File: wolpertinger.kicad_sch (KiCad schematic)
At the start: 57 parts, among them IC1 TL074, IC2 TL074, K1 FRT5, K2 FRT5, Q1 BC549, T1 IN LEFT, T2 IN RIGHT, T3 SWT, T4 SWT, T5 OUT LEFT, T6 OUT RIGHT, T7 LED+, T8 LED-, U1 4093, U2 VTL5C, U3 VTL5C, U4 VTL5C, U5 VTL5C

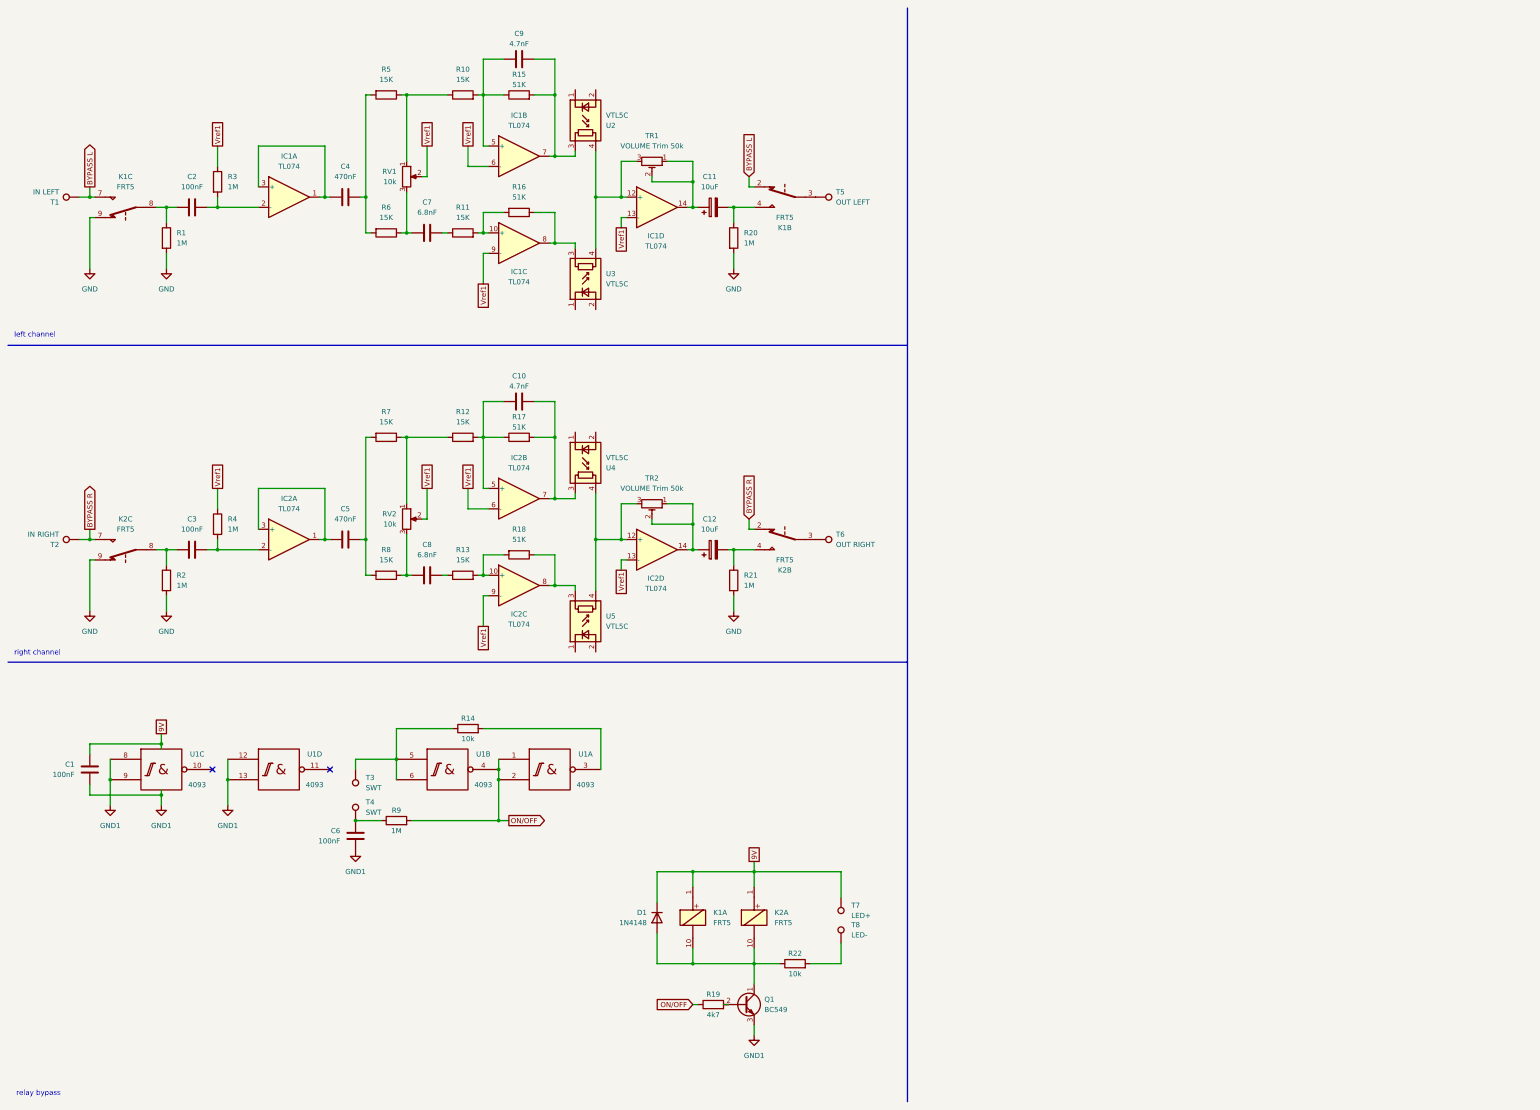
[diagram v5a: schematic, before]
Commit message: add power supply
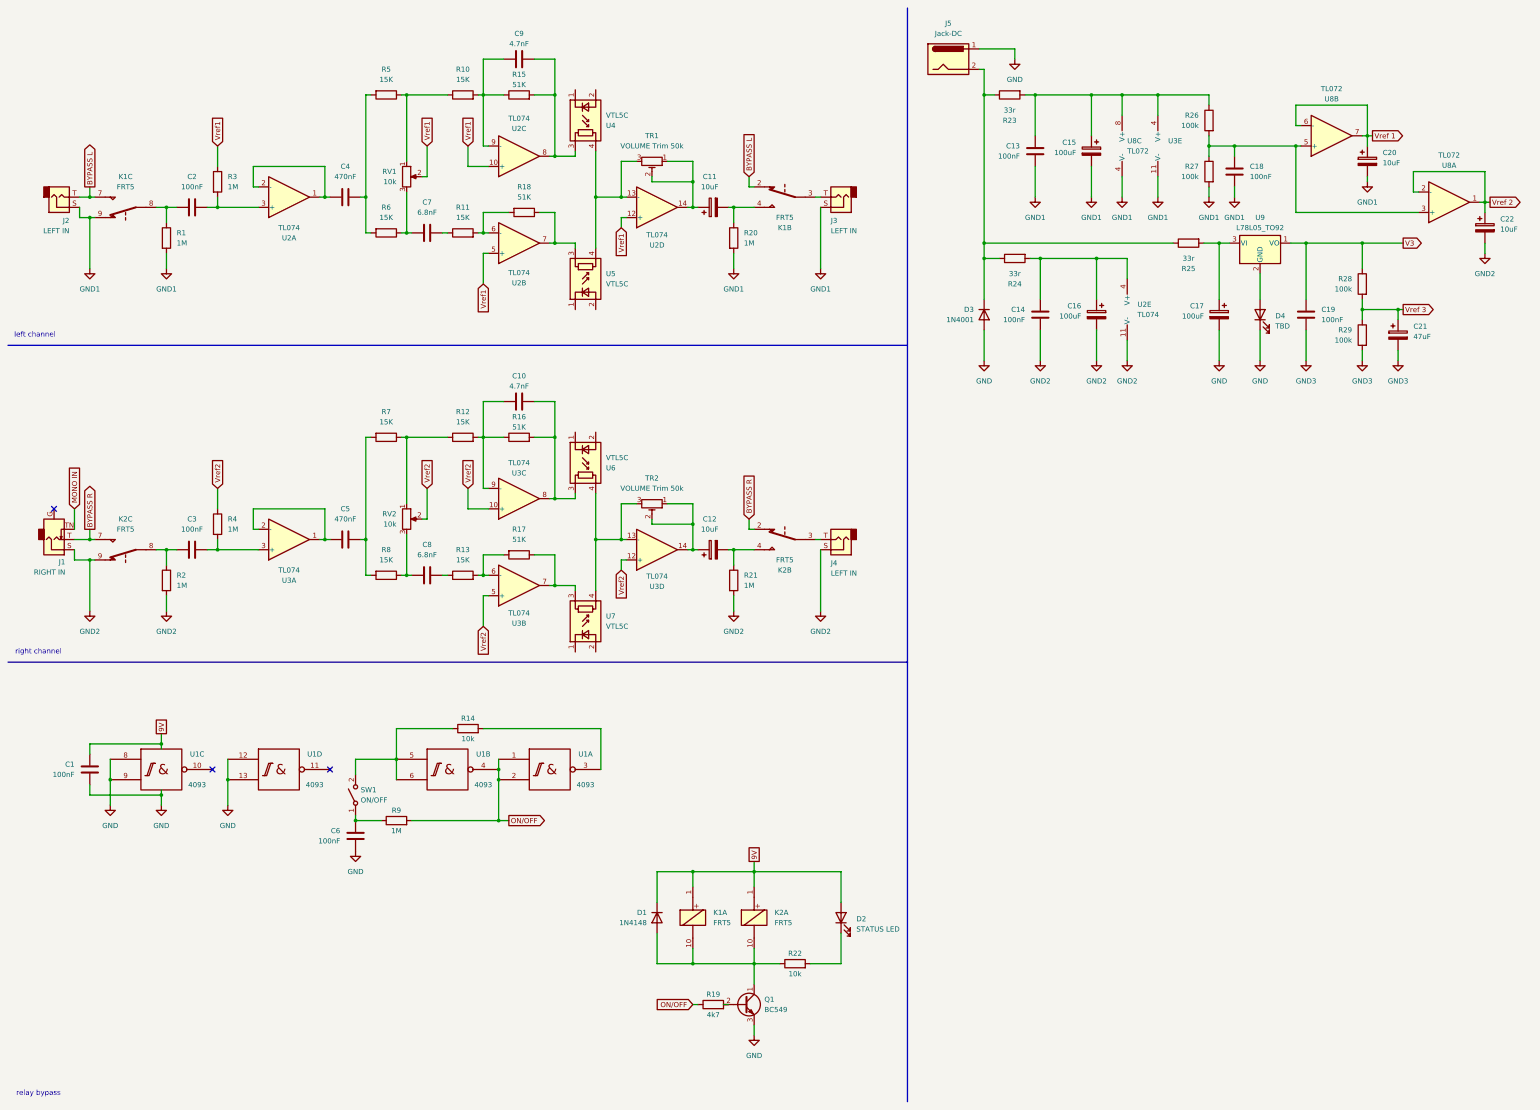
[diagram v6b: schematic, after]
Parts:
- removed IC1, IC2: TL074, Package_DIP:CERDIP-14_W7.62mm_SideBrazed_LongPads_Socket, symbol Amplifier_Operational:TL074
- removed T1: IN LEFT, Connector_Wire:SolderWire-0.5sqmm_1x01_D0.9mm_OD2.1mm, symbol Connector:TestPoint
- removed T2: IN RIGHT, Connector_Wire:SolderWire-0.5sqmm_1x01_D0.9mm_OD2.1mm, symbol Connector:TestPoint
- removed T3, T4: SWT, Connector_Wire:SolderWire-0.5sqmm_1x01_D0.9mm_OD2.1mm, symbol Connector:TestPoint
- removed T5: OUT LEFT, Connector_Wire:SolderWire-0.5sqmm_1x01_D0.9mm_OD2.1mm, symbol Connector:TestPoint
- removed T6: OUT RIGHT, Connector_Wire:SolderWire-0.5sqmm_1x01_D0.9mm_OD2.1mm, symbol Connector:TestPoint
- removed T7: LED+, Connector_Wire:SolderWire-0.5sqmm_1x01_D0.9mm_OD2.1mm, symbol Connector:TestPoint
- removed T8: LED-, Connector_Wire:SolderWire-0.5sqmm_1x01_D0.9mm_OD2.1mm, symbol Connector:TestPoint
- added C13, C14, C18, C19: 100nF, symbol Device:C
- added C15, C16, C17: 100uF, symbol Device:C_Polarized
- added C20, C22: 10uF, symbol Device:C_Polarized
- added C21: 47uF, symbol Device:C_Polarized
- added D2: STATUS LED, symbol Device:LED
- added D3: 1N4001, Diode_THT:D_DO-41_SOD81_P10.16mm_Horizontal, symbol Diode:1N4001
- added D4: TBD, symbol Device:LED
- added J1: RIGHT IN, symbol Connector_Audio:NRJ4HH-1
- added J2, J3, J4: LEFT IN, symbol Connector_Audio:NJ2FD-V
- added J5: Jack-DC, symbol Connector:Jack-DC
- added R23, R24, R25: 33r, Resistor_THT:R_Axial_DIN0207_L6.3mm_D2.5mm_P7.62mm_Horizontal, symbol Device:R
- added R26, R27, R28, R29: 100k, Resistor_THT:R_Axial_DIN0207_L6.3mm_D2.5mm_P7.62mm_Horizontal, symbol Device:R
- added SW1: ON/OFF, symbol Switch:SW_SPST
- added U2, U3: TL074, symbol Amplifier_Operational:TL074
- added U8: TL072, symbol Amplifier_Operational:TL072
- added U9: L78L05_TO92, Package_TO_SOT_THT:TO-92_Inline, symbol Regulator_Linear:L78L05_TO92
- renumbered R17 to R16, R18 to R17, R16 to R18, U2 to U4, U3 to U5, U4 to U6, U5 to U7
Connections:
- net BYPASS L: now also J2.T
- net BYPASS R: now also J1.T
- net GND: now also C1.2, C6.2, Q1.3 (E), U1.12, U1.13, U1.7 (Vss), U1.7 (Vss), U1.7 (Vss), U1.7 (Vss), U1.8, U1.9, C17.2, D3.2 (A), D4.1 (K), J5.1; no longer K1.9, K2.9, R1.2, R2.2, R20.2, R21.2
- net GND1: now also K1.9, R1.2, R20.2, C13.1, C15.2, C18.1, C20.2, J2.S, J3.S, R27.2, U3.11 (V-), U8.4 (V-); no longer C1.2, C6.2, Q1.3 (E), U1.12, U1.13, U1.7 (Vss), U1.7 (Vss), U1.7 (Vss), U1.7 (Vss), U1.8, U1.9
- net Vdd: now also D2.2 (A)
- net Vref1: now also U2.10 (+), U2.12 (+), U2.5 (+); no longer R4.1, RV2.2
- net at C9.1, R10.2, R15.1: now also U2.9 (-)
- net at K2.3: now also J4.T
- net at TR2.3, U6.4, U7.4: now also U3.13 (-)
- net at C12.1, TR2.1, TR2.2: now also U3.14
- net at C9.2, R15.2, U4.3: now also U2.8
- net at TR1.3, U4.4, U5.4: now also U2.13 (-)
- net at C4.1: now also U2.1, U2.2 (-)
- net at C2.2, R3.2: now also U2.3 (+)
- net at R14.1, U1.5, U1.6: now also SW1.2 (B)
- net at R17.1, U7.3: now also U3.7
- net at C10.2, R16.2, U6.3: now also U3.8
- net at C5.1: now also U3.1, U3.2 (-)
- net at C3.2, R4.2: now also U3.3 (+)
- net at R22.2: now also D2.1 (K)
- net at C6.1, R9.1: now also SW1.1 (A)
- net at K1.3: now also J3.T
- net at R13.2, R17.2: now also U3.6 (-)
- net at C11.1, TR1.1, TR1.2: now also U2.14
- net at R11.2, R18.2: now also U2.6 (-)
- net at R18.1, U5.3: now also U2.7
- net at C10.1, R12.2, R16.1: now also U3.9 (-)
- new net: C18.2, R26.2, R27.1, U8.3 (+), U8.5 (+)
- new net: D4.2 (A), U9.2 (GND)
- new net: C17.1, R25.2, U9.3 (VI)
- new net: C13.2, C15.1, R23.2, R26.1, U3.4 (V+), U8.8 (V+)
- new net: D3.1 (K), J5.2, R23.1, R24.1, R25.1
- new net: C14.2, C16.1, R24.2, U2.4 (V+)
- new net GND2: C14.1, C16.2, C22.2, J1.S, J4.S, K2.9, R2.2, R21.2, U2.11 (V-)
- new net GND3: C19.1, C21.2, R29.2
- new net MONO IN: J1.TN
- new net V3: C19.2, R28.1, U9.1 (VO)
- new net Vref 1: C20.1, U8.6 (-), U8.7
- new net Vref 2: C22.1, U8.1, U8.2 (-)
- new net Vref 3: C21.1, R28.2, R29.1
- new net Vref2: R4.1, RV2.2, U3.10 (+), U3.12 (+), U3.5 (+)
- no-connect marks 2 -> 3
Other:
- moved on the sheet: R18

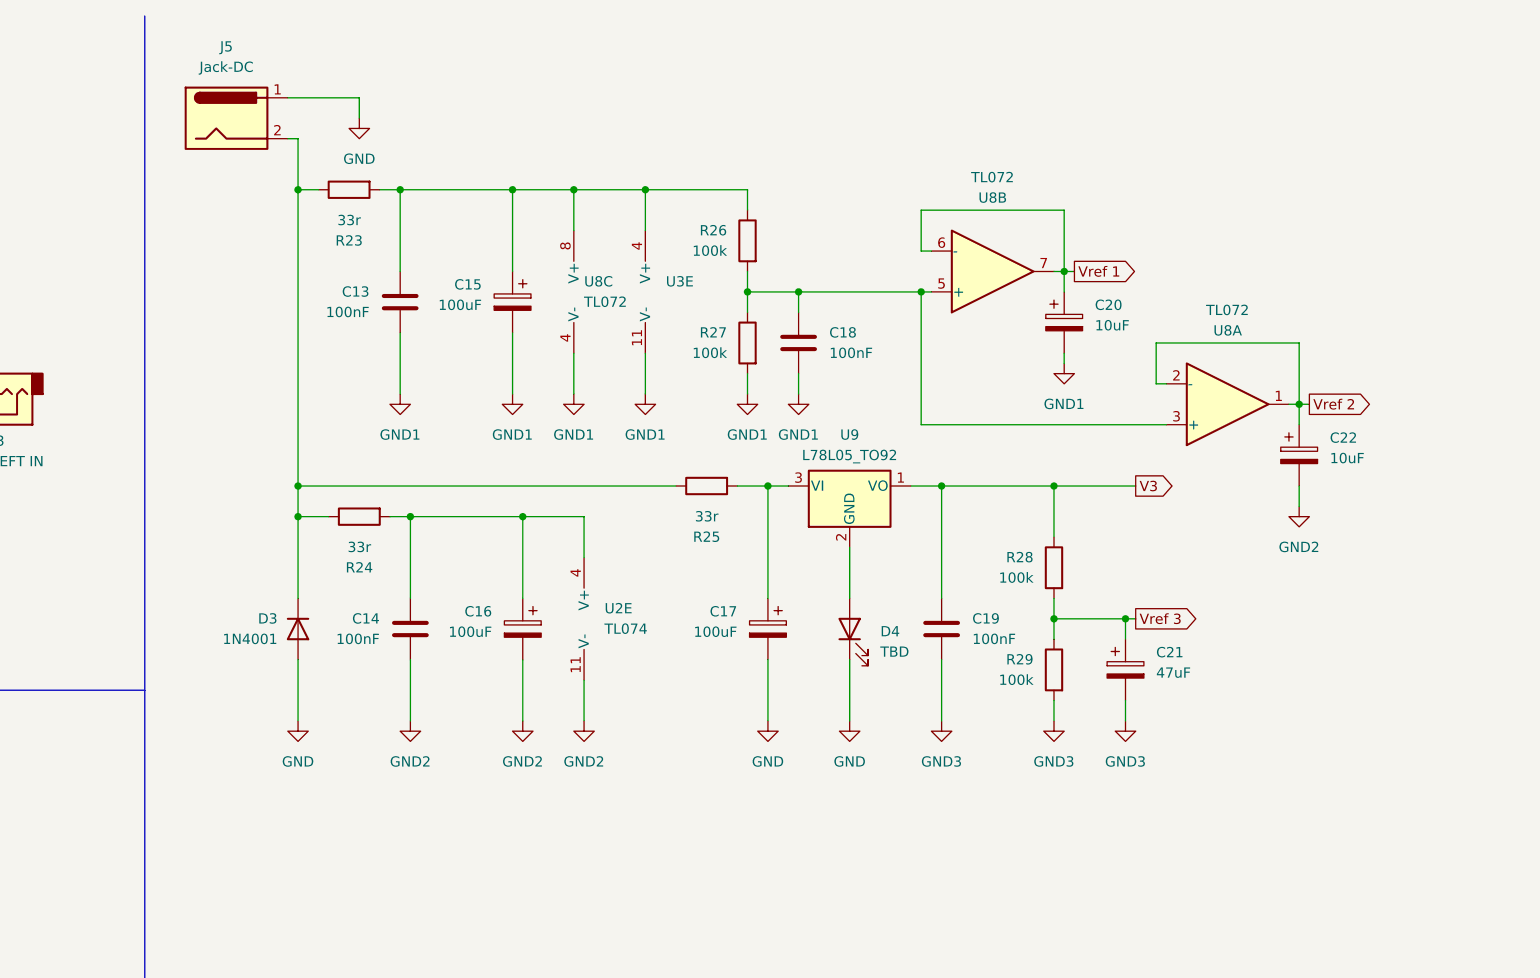
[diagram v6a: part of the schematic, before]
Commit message: add different power supply grounds
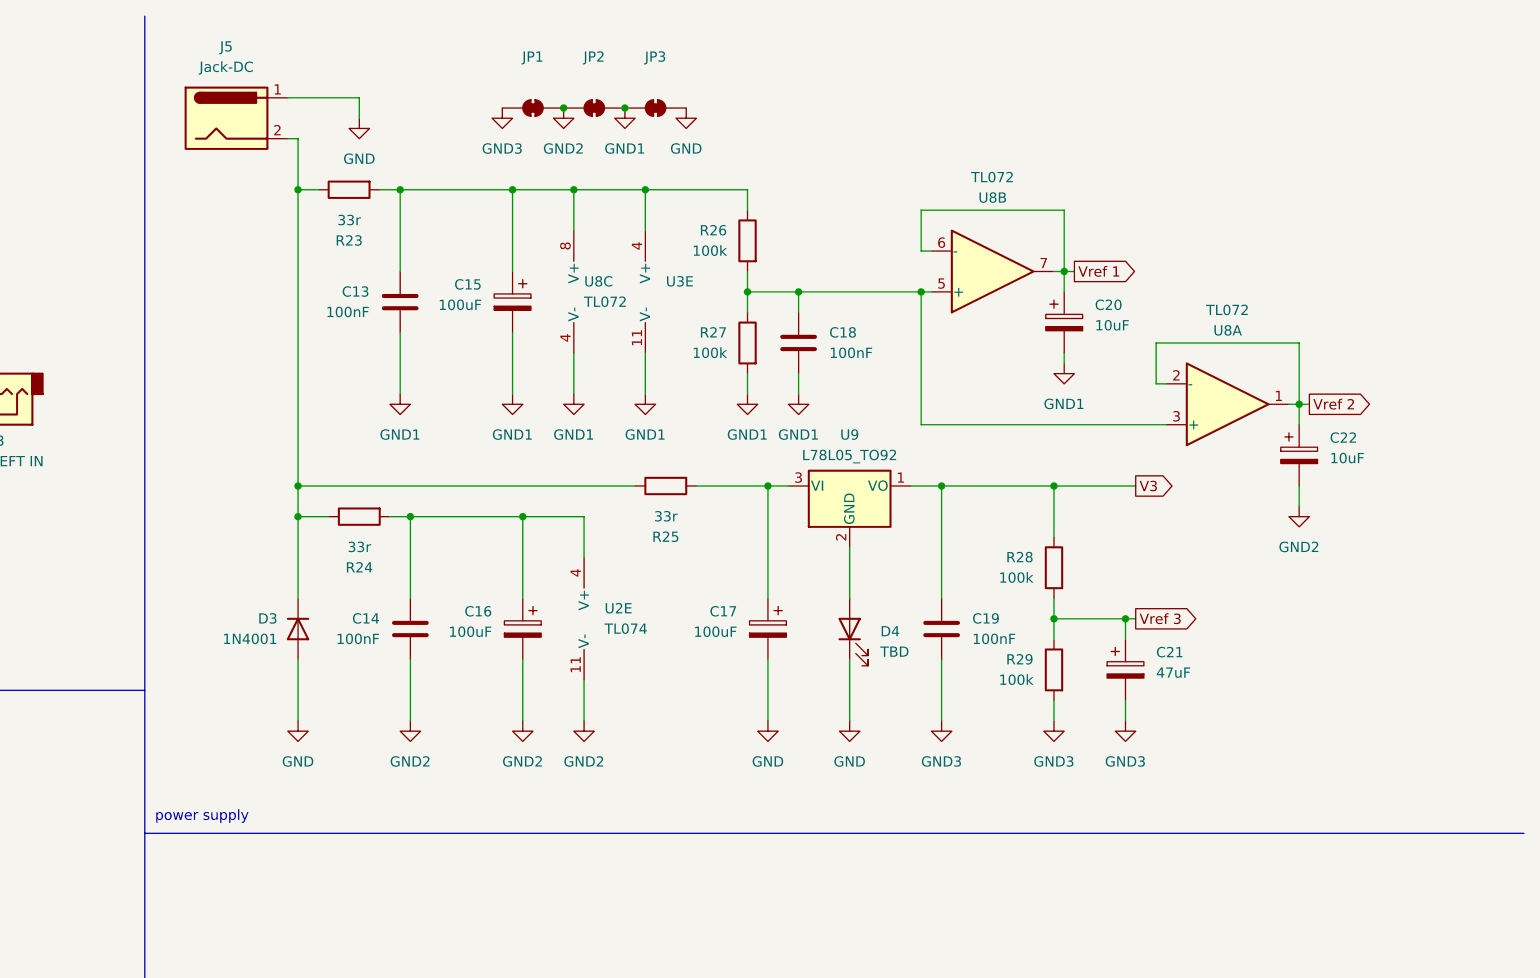
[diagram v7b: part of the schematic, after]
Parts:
- added JP1, JP2, JP3: ~, Jumper:SolderJumper-2_P1.3mm_Bridged_RoundedPad1.0x1.5mm, symbol Jumper:SolderJumper_2_Bridged
- D4: footprint (none) -> LED_THT:LED_D3.0mm
- U2, U3: footprint (none) -> Package_DIP:CERDIP-14_W7.62mm_SideBrazed_LongPads_Socket
- U8: footprint (none) -> Package_DIP:DIP-8_W7.62mm_Socket_LongPads
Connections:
- net GND: now also JP3.2 (B)
- net GND1: now also JP2.2 (B), JP3.1 (A)
- net GND2: now also JP1.2 (B), JP2.1 (A)
- net GND3: now also JP1.1 (A)
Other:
- note added: "power supply"
- moved on the sheet: R25
